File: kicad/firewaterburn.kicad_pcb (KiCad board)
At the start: 2 copper layers, 105.2 x 79 mm, 72 parts, among them J1 AudioJack2_SwitchT, J2 AudioJack2_SwitchT, J3 Conn_01x03, J4 AudioJack2_SwitchT, J5 AudioJack2_SwitchT, J6 AudioJack2_SwitchT, J7 AudioJack2_SwitchT, J8 RVT50HQBNWC00, P1 USB_C_Plug_USB2.0, Q1 DMN61D9UWQ-13, Q2 DMP31D0U-7, Q5 DMN2004WK-7, U1 RT9471GQW, U2 MCP1663T-E/MNY, U3 MCP1603-330I/MC, U4 BL654, U5 CP2102N-Axx-xQFN28

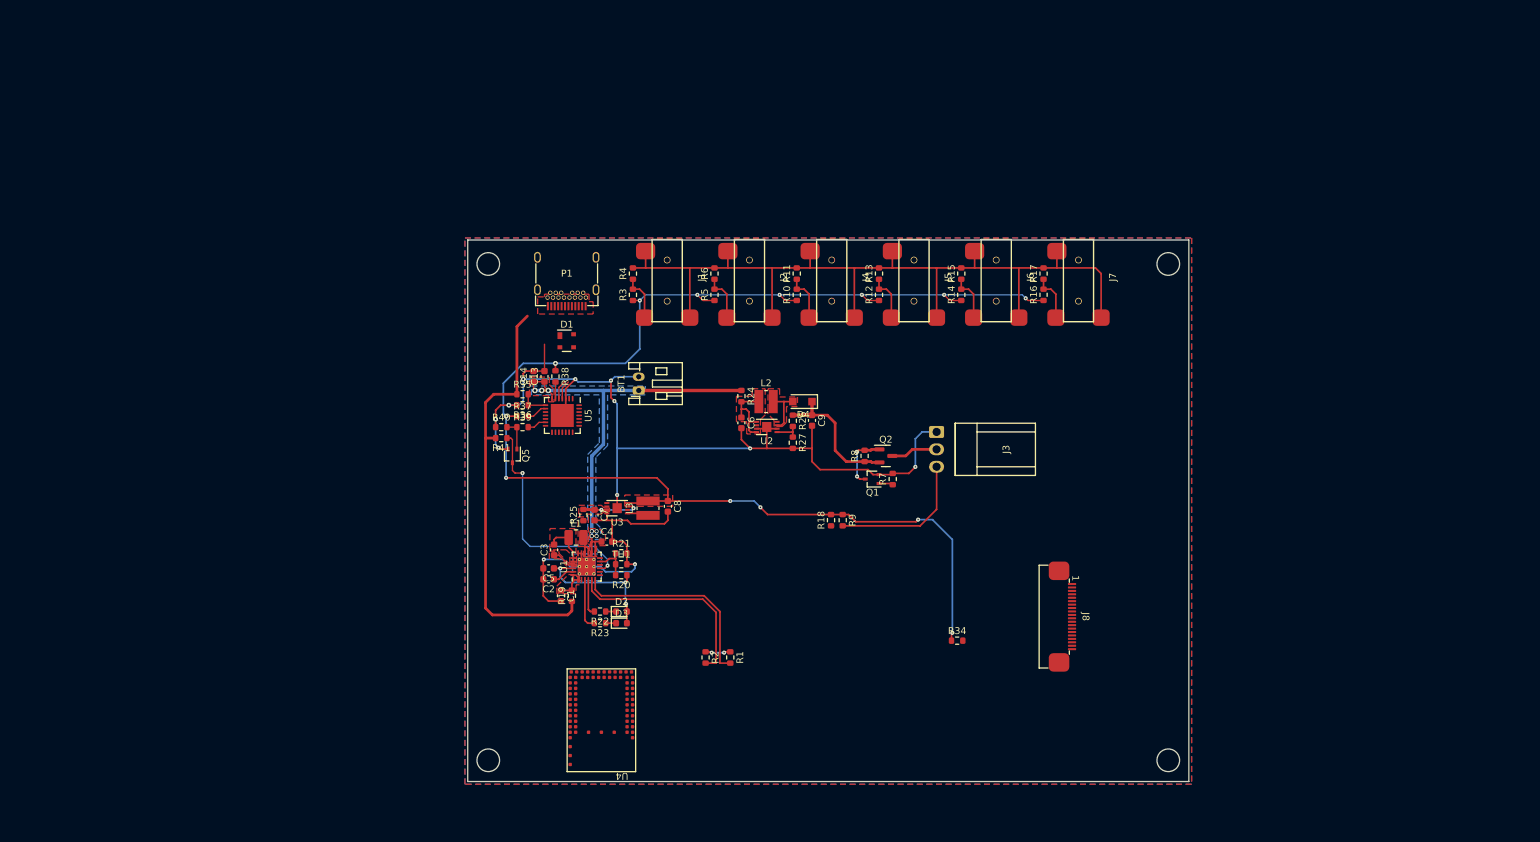
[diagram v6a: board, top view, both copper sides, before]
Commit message: add all digikeys numbers to schematic
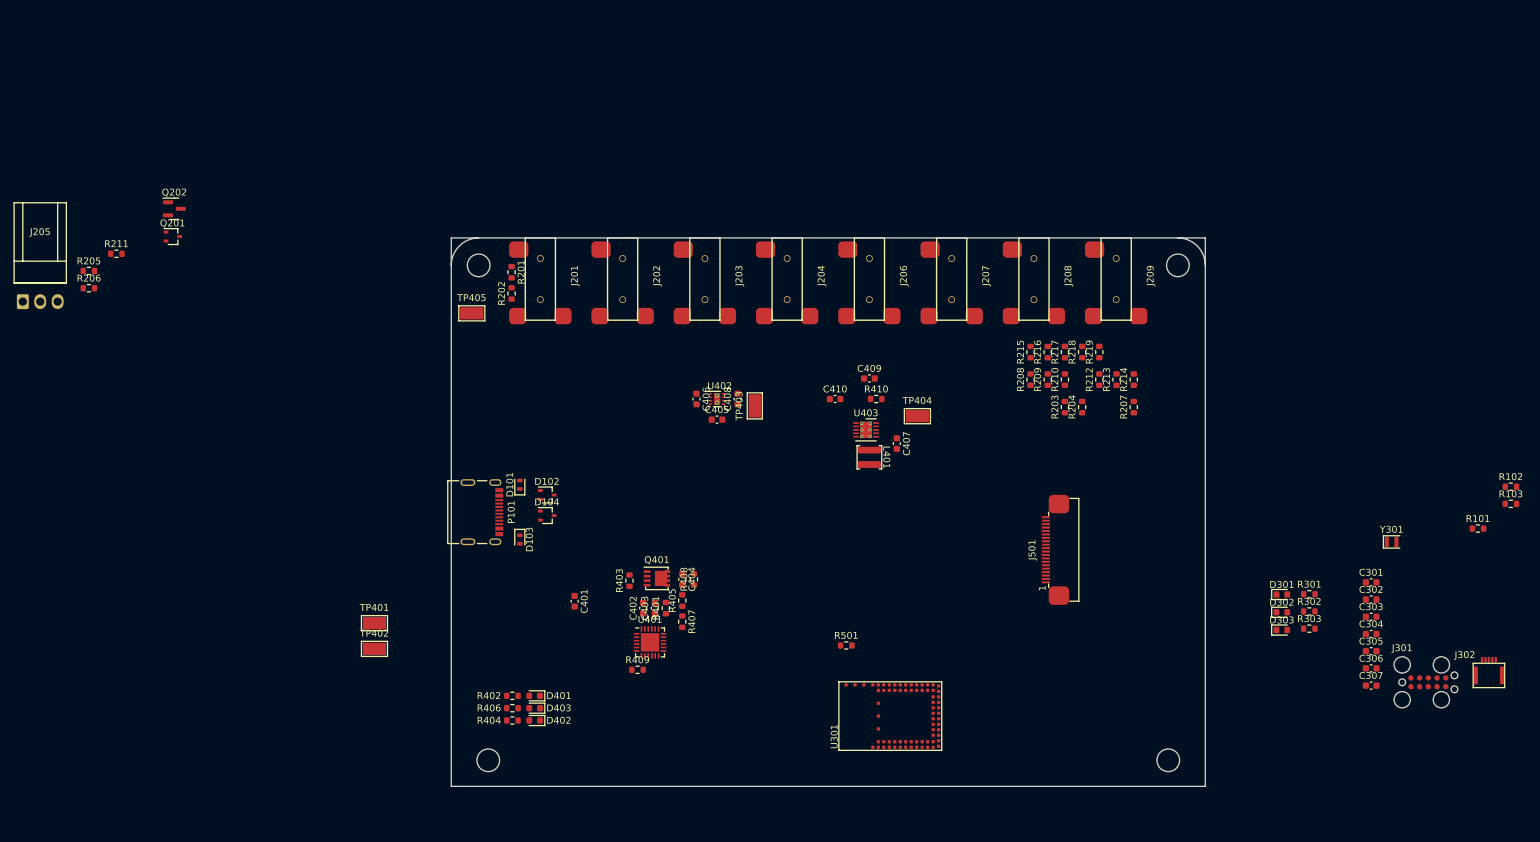
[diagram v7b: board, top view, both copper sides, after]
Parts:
- removed BT1: Battery_Cell, Connector_JST:JST_PH_S2B-PH-K_1x02_P2.00mm_Horizontal
- removed C1: 1µ, Capacitor_SMD:C_0603_1608Metric
- removed C13, C5, C7, C8: 4,7µ, Capacitor_SMD:C_0603_1608Metric
- removed C14: 100n, Capacitor_SMD:C_0603_1608Metric
- removed C2, C4, C6, C9: 10µ, Capacitor_SMD:C_0603_1608Metric
- removed C3: 47nF, Capacitor_SMD:C_0603_1608Metric
- removed D1: SP0503BAHTG, Package_TO_SOT_SMD:SOT-143
- removed D2, D3: LED, LED_SMD:LED_0603_1608Metric
- removed D4: PMEG4010ER, Diode_SMD:D_SOD-123F
- removed J1, J2, J4, J5, J6, J7: AudioJack2_SwitchT, mylib_connector:MJ-2523
- removed J3: Conn_01x03, z_connector:Molex_KK-254_AE-6410-03A_1x03_P2.54mm_Vertical
- removed J8: RVT50HQBNWC00, mylib_connector:FPC_BOTTOM_20POS_Würth_68712014522
- removed L1: 1µ, Inductor_SMD:L_1008_2520Metric
- removed L2, L3: 4µ7, Inductor_SMD:L_Wuerth_MAPI-3015
- removed P1: USB_C_Plug_USB2.0, mylib_connector:USB_C_Receptacle_Amphenol_12401548E4-2A
- removed Q1: DMN61D9UWQ-13, Package_TO_SOT_SMD:SOT-323_SC-70
- removed Q2: DMP31D0U-7, Package_TO_SOT_SMD:SOT-23
- removed Q5: DMN2004WK-7, Package_TO_SOT_SMD:SOT-323_SC-70
- removed R1, R2: 1k, Resistor_SMD:R_0603_1608Metric
- removed R10, R12, R14, R16, R3, R5: 4k42, Resistor_SMD:R_0603_1608Metric
- removed R11, R13, R15, R17, R4, R6: 3k4, Resistor_SMD:R_0603_1608Metric
- removed R18, R41, R9: 10k, Resistor_SMD:R_0603_1608Metric
- removed R19, R24, R25, R34, R38, R39: 0R, Resistor_SMD:R_0603_1608Metric
- removed R20: 5k23, Resistor_SMD:R_0603_1608Metric
- removed R21: 30k1, Resistor_SMD:R_0603_1608Metric
- removed R22, R23: 2k2, Resistor_SMD:R_0603_1608Metric
- removed R26: 1050k, Resistor_SMD:R_0603_1608Metric
- removed R27: 120k, Resistor_SMD:R_0603_1608Metric
- removed R35: 22k1, Resistor_SMD:R_0603_1608Metric
- removed R36: 47k5, Resistor_SMD:R_0603_1608Metric
- removed R37: 2k, Resistor_SMD:R_0603_1608Metric
- removed R40: 1M, Resistor_SMD:R_0603_1608Metric
- removed R7, R8: 4k7, Resistor_SMD:R_0603_1608Metric
- removed TH1: NTCG163JH103JT1, Resistor_SMD:R_0603_1608Metric
- removed U1: RT9471GQW, mylib_ic:WQFN-24-1EP_4x4mm_P0.5mm_EP2.6x2.6mm_ThermalVias
- removed U2: MCP1663T-E/MNY, Package_DFN_QFN:DFN-8-1EP_3x2mm_P0.5mm_EP1.36x1.46mm
- removed U3: MCP1603-330I/MC, Package_DFN_QFN:DFN-8-1EP_3x2mm_P0.5mm_EP1.36x1.46mm
- removed U4: BL654, mylib_ic:BL654
- removed U5: CP2102N-Axx-xQFN28, Package_DFN_QFN:QFN-28-1EP_5x5mm_P0.5mm_EP3.35x3.35mm
- added C301: 10µ, Capacitor_SMD:C_0603_1608Metric, F.Cu at (229.2, 110.2)
- added C302: 100nF, Capacitor_SMD:C_0603_1608Metric, F.Cu at (229.2, 112.8)
- added C303: 4µ7, Capacitor_SMD:C_0603_1608Metric, F.Cu at (229.2, 115.3)
- added C304: 300p, Capacitor_SMD:C_0603_1608Metric, F.Cu at (229.2, 117.8)
- added C305: 9p, Capacitor_SMD:C_0603_1608Metric, F.Cu at (229.2, 120.3)
- added C306: 300p, Capacitor_SMD:C_0603_1608Metric, F.Cu at (229.2, 122.8)
- added C307: 9p, Capacitor_SMD:C_0603_1608Metric, F.Cu at (229.2, 125.3)
- added C401: 1µ, Capacitor_SMD:C_0603_1608Metric, F.Cu at (113.0, 113.0)
- added C402: 1µ, Capacitor_SMD:C_0603_1608Metric, F.Cu at (123.0, 114.0)
- added C403: 1µ, Capacitor_SMD:C_0603_1608Metric, F.Cu at (124.7, 114.0)
- added C404: 100nF, Capacitor_SMD:C_0603_1608Metric, F.Cu at (128.7, 109.8)
- added C405: 10µ, Capacitor_SMD:C_0603_1608Metric, F.Cu at (133.8, 86.5)
- added C406: 1µ, Capacitor_SMD:C_0603_1608Metric, F.Cu at (130.8, 83.5)
- added C407: 0.47µ, Capacitor_SMD:C_0603_1608Metric, F.Cu at (160.0, 90.0)
- added C408: 10µ, Capacitor_SMD:C_0603_1608Metric, F.Cu at (136.8, 83.5)
- added C409: 22µ, Capacitor_SMD:C_0603_1608Metric, F.Cu at (156.0, 80.5)
- added C410: 4µ7, Capacitor_SMD:C_0603_1608Metric, F.Cu at (151.0, 83.5)
- added D101: ESDA25P35, mylib_ic:D_0604_1610Metric, F.Cu at (105.0, 96.0)
- added D102: ESDA25W, Package_TO_SOT_SMD:SOT-323_SC-70, F.Cu at (109.0, 97.5)
- added D103: ESDA25P35, mylib_ic:D_0604_1610Metric, F.Cu at (105.0, 104.0)
- added D104: ESDA25W, Package_TO_SOT_SMD:SOT-323_SC-70, F.Cu at (109.0, 100.5)
- added D301: LED, LED_SMD:LED_0603_1608Metric, F.Cu at (216.2, 112.0)
- added D302: LED, LED_SMD:LED_0603_1608Metric, F.Cu at (216.2, 114.6)
- added D303: LED, LED_SMD:LED_0603_1608Metric, F.Cu at (216.2, 117.2)
- added D401: LED, LED_SMD:LED_0603_1608Metric, F.Cu at (107.2, 126.8)
- added D402: LED, LED_SMD:LED_0603_1608Metric, F.Cu at (107.2, 130.4)
- added D403: LED, LED_SMD:LED_0603_1608Metric, F.Cu at (107.2, 128.6)
- added J201: AudioJack2_SwitchT, mylib_connector:MJ-2523, F.Cu at (108.0, 60.0)
- added J202: AudioJack2_SwitchT, mylib_connector:MJ-2523, F.Cu at (120.0, 60.0)
- added J203: AudioJack2_SwitchT, mylib_connector:MJ-2523, F.Cu at (132.0, 60.0)
- added J204: AudioJack2_SwitchT, mylib_connector:MJ-2523, F.Cu at (144.0, 60.0)
- added J205: Conn_01x03, mylib_connector:Molex_KK-254_AE-6410-03A_1x03_P2.54mm_Vertical, F.Cu at (32.5, 69.3)
- added J206: AudioJack2_SwitchT, mylib_connector:MJ-2523, F.Cu at (156.0, 60.0)
- added J207: AudioJack2_SwitchT, mylib_connector:MJ-2523, F.Cu at (168.0, 60.0)
- added J208: AudioJack2_SwitchT, mylib_connector:MJ-2523, F.Cu at (180.0, 60.0)
- added J209: AudioJack2_SwitchT, mylib_connector:MJ-2523, F.Cu at (192.0, 60.0)
- added J301: TC-2050, mylib_connector:TC-2050, F.Cu at (233.7, 124.8)
- added J302: Conn_01x05, mylib_connector:Easy-On 51281-5, F.Cu at (246.4, 123.8)
- added J501: RVT50HQBNWC00, mylib_connector:FPC_BOTTOM_20POS_Würth_68712014522, F.Cu at (181.8, 105.5)
- added L401: 15µ, mylib_ic:L_TDK_VLS6045EX_VLS6045AF, F.Cu at (156.0, 92.0)
- added P101: USB_C_Plug_USB2.0, mylib_connector:USB_C_Receptacle_Molex_C_24P_SMD_RA, F.Cu at (102.0, 100.0)
- added Q201: DMN61D9UWQ-13, Package_TO_SOT_SMD:SOT-323_SC-70, F.Cu at (54.4, 59.8)
- added Q202: DMP31D0U-7, Package_TO_SOT_SMD:SOT-23, F.Cu at (54.6, 55.8)
- added Q401: SI7421DN-T1-E3, Package_SO:Vishay_PowerPAK_1212-8_Single, F.Cu at (125.0, 109.7)
- added R101: 4k7, Resistor_SMD:R_0603_1608Metric, F.Cu at (244.8, 102.4)
- added R102: 4k7, Resistor_SMD:R_0603_1608Metric, F.Cu at (249.6, 96.3)
- added R103: 4k7, Resistor_SMD:R_0603_1608Metric, F.Cu at (249.6, 98.8)
- added R201: 4k42, Resistor_SMD:R_0603_1608Metric, F.Cu at (103.8, 65.0)
- added R202: 3k4, Resistor_SMD:R_0603_1608Metric, F.Cu at (103.8, 68.1)
- added R203: 4k42, Resistor_SMD:R_0603_1608Metric, F.Cu at (184.5, 84.7)
- added R204: 3k4, Resistor_SMD:R_0603_1608Metric, F.Cu at (187.0, 84.7)
- added R205: 4k7, Resistor_SMD:R_0603_1608Metric, F.Cu at (42.1, 64.8)
- added R206: 4k7, Resistor_SMD:R_0603_1608Metric, F.Cu at (42.1, 67.3)
- added R207: 4k42, Resistor_SMD:R_0603_1608Metric, F.Cu at (194.6, 84.7)
- added R208: 3k4, Resistor_SMD:R_0603_1608Metric, F.Cu at (179.5, 80.7)
- added R209: 4k42, Resistor_SMD:R_0603_1608Metric, F.Cu at (182.0, 80.7)
- added R210: 3k4, Resistor_SMD:R_0603_1608Metric, F.Cu at (184.5, 80.7)
- added R211: 10k, Resistor_SMD:R_0603_1608Metric, F.Cu at (46.1, 62.3)
- added R212: 4k42, Resistor_SMD:R_0603_1608Metric, F.Cu at (189.5, 80.7)
- added R213: 3k4, Resistor_SMD:R_0603_1608Metric, F.Cu at (192.1, 80.7)
- added R214: 4k42, Resistor_SMD:R_0603_1608Metric, F.Cu at (194.6, 80.7)
- added R215: 3k4, Resistor_SMD:R_0603_1608Metric, F.Cu at (179.5, 76.7)
- added R216: 4k42, Resistor_SMD:R_0603_1608Metric, F.Cu at (182.0, 76.7)
- added R217: 3k4, Resistor_SMD:R_0603_1608Metric, F.Cu at (184.5, 76.7)
- added R218: 4k42, Resistor_SMD:R_0603_1608Metric, F.Cu at (187.0, 76.7)
- added R219: 3k4, Resistor_SMD:R_0603_1608Metric, F.Cu at (189.5, 76.7)
- added R301: 1k, Resistor_SMD:R_0603_1608Metric, F.Cu at (220.2, 112.0)
- added R302: 1k, Resistor_SMD:R_0603_1608Metric, F.Cu at (220.2, 114.5)
- added R303: 1k, Resistor_SMD:R_0603_1608Metric, F.Cu at (220.2, 117.0)
- added R401: 1k, Resistor_SMD:R_0603_1608Metric, F.Cu at (126.3, 114.0)
- added R402: 1k, Resistor_SMD:R_0603_1608Metric, F.Cu at (103.9, 126.8)
- added R403: 100k, Resistor_SMD:R_0603_1608Metric, F.Cu at (121.0, 110.0)
- added R404: 1k, Resistor_SMD:R_0603_1608Metric, F.Cu at (103.9, 130.4)
- added R405: 100, Resistor_SMD:R_0603_1608Metric, F.Cu at (128.7, 112.9)
- added R406: 1k, Resistor_SMD:R_0603_1608Metric, F.Cu at (103.9, 128.6)
- added R407: 22k, Resistor_SMD:R_0603_1608Metric, F.Cu at (128.7, 116.0)
- added R408: 1k, Resistor_SMD:R_0603_1608Metric, F.Cu at (130.4, 109.8)
- added R409: 100k, Resistor_SMD:R_0603_1608Metric, F.Cu at (122.2, 123.0)
- added R410: 215k, Resistor_SMD:R_0603_1608Metric, F.Cu at (157.0, 83.5)
- added R501: 0R, Resistor_SMD:R_0603_1608Metric, F.Cu at (152.6, 119.5)
- added TP401: TestPoint, TestPoint:TestPoint_Keystone_5015_Micro-Minature, F.Cu at (83.8, 116.2)
- added TP402: TestPoint, TestPoint:TestPoint_Keystone_5015_Micro-Minature, F.Cu at (83.8, 120.0)
- added TP403: TestPoint, TestPoint:TestPoint_Keystone_5015_Micro-Minature, F.Cu at (139.3, 84.5)
- added TP404: TestPoint, TestPoint:TestPoint_Keystone_5015_Micro-Minature, F.Cu at (163.0, 86.0)
- added TP405: TestPoint, TestPoint:TestPoint_Keystone_5015_Micro-Minature, F.Cu at (98.0, 71.0)
- added U301: BL654, mylib_ic:BL654, F.Cu at (166.6, 124.8)
- added U401: STUSB4500QTR, Package_DFN_QFN:QFN-24-1EP_4x4mm_P0.5mm_EP2.7x2.7mm, F.Cu at (124.0, 119.0)
- added U402: LM2775DSG, Package_SON:WSON-8-1EP_2x2mm_P0.5mm_EP0.9x1.6mm_ThermalVias, F.Cu at (133.8, 83.5)
- added U403: LT3973-3.3, Package_DFN_QFN:DFN-10-1EP_3x3mm_P0.5mm_EP1.65x2.38mm_ThermalVias, F.Cu at (155.5, 88.0)
- added Y301: Crystal, mylib_ic:CM8V-T1A-2Pin_2.0x1.2mm, F.Cu at (232.2, 104.3)
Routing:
- net GND: track 307.0 -> 0.00 mm, vias 12 -> 0
- net +3V3: track 211.8 -> 0.00 mm, vias 15 -> 0
- net VAA: track 65.7 -> 0.00 mm, vias 7 -> 0
- net VBUS: track 63.2 -> 0.00 mm
- net /USB<->UART/CHREN: track 32.4 -> 0.00 mm, vias 2 -> 0
- net /power unit/CHARGER_SCL: track 30.0 -> 0.00 mm
- net /power unit/CHARGER_SDA: track 29.9 -> 0.00 mm
- net Net-(C5-Pad1): track 21.1 -> 0.00 mm, vias 3 -> 0
- net /OUTPUT/TACHO: track 20.9 -> 0.00 mm
- net +12V: track 19.8 -> 0.00 mm
- net Net-(C6-Pad1): track 11.1 -> 0.00 mm
- net Net-(C7-Pad1): track 9.23 -> 0.00 mm, vias 2 -> 0
- net Net-(Q1-Pad3): track 8.36 -> 0.00 mm, vias 2 -> 0
- net /power unit/~{PG}: track 7.45 -> 0.00 mm
- net Net-(D4-Pad2): track 7.09 -> 0.00 mm
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- removed copper zone on F.Cu, net +3V3
- removed copper zone on B.Cu, net GND
- removed copper zone on F.Cu, net GND
- removed copper zone on F.Cu, net Net-(C1-Pad1)
- removed copper zone on F.Cu, net Net-(C3-Pad1)
- removed copper zone on F.Cu, net Net-(C3-Pad2)
- removed copper zone on F.Cu, net Net-(C6-Pad1)
- removed copper zone on F.Cu, net Net-(C7-Pad1)
- removed copper zone on F.Cu, net Net-(D4-Pad2)
- removed copper zone on B.Cu, net VAA
- removed copper zone on F.Cu, net VAA
- removed copper zone on F.Cu, net VS
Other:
- board size 105.2 x 79 mm -> 110 x 80 mm

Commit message: wip
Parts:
- removed D103: ESDA25P35, mylib_ic:D_0604_1610Metric
- removed D104: ESDA25W, Package_TO_SOT_SMD:SOT-323_SC-70
- removed J208, J209: AudioJack2_SwitchT, mylib_connector:MJ-2523
- removed R216, R218: 4k42, Resistor_SMD:R_0603_1608Metric
- removed R217, R219: 3k4, Resistor_SMD:R_0603_1608Metric
- added U101: TPD4E02B04DQA, Package_SON:USON-10_2.5x1.0mm_P0.5mm, F.Cu at (90.2, 80.8)
- C304: value 300p -> 9p
- C307: value 9p -> 300p
- C401: value 1µ -> 100nF
- C402: value 1µ -> 0.47µ
- C404: value 100nF -> 4µ7
- C405: value 10µ -> 22µ
- C407: value 0.47µ -> 1µ
- C409: value 22µ -> 1µ
- C410: value 4µ7 -> 10µ
- D102: value ESDA25W -> ESDA25P35; footprint Package_TO_SOT_SMD:SOT-323_SC-70 -> mylib_ic:D_0604_1610Metric
- J205: value Conn_01x03 -> AudioJack2_SwitchT; footprint mylib_connector:Molex_KK-254_AE-6410-03A_1x03_P2.54mm_Vertical -> mylib_connector:MJ-2523
- J207: value AudioJack2_SwitchT -> Conn_01x03; footprint mylib_connector:MJ-2523 -> mylib_connector:Molex_KK-254_AE-6410-03A_1x03_P2.54mm_Vertical
- J301: value TC-2050 -> Conn_01x05; footprint mylib_connector:TC-2050 -> mylib_connector:Easy-On 51281-5
- J302: value Conn_01x05 -> TC-2050; footprint mylib_connector:Easy-On 51281-5 -> mylib_connector:TC-2050
- Q201: value DMN61D9UWQ-13 -> DMP31D0U-7; footprint Package_TO_SOT_SMD:SOT-323_SC-70 -> Package_TO_SOT_SMD:SOT-23
- Q202: value DMP31D0U-7 -> DMN61D9UWQ-13; footprint Package_TO_SOT_SMD:SOT-23 -> Package_TO_SOT_SMD:SOT-323_SC-70
- R202, R208: value 3k4 -> 4k42
- R205, R206: value 4k7 -> 3k4
- R211: value 10k -> 3k4
- R212: value 4k42 -> 3k4
- R213, R215: value 3k4 -> 4k7
- R214: value 4k42 -> 10k
- R402: value 1k -> 100k
- R403, R409: value 100k -> 1k
- R404: value 1k -> 100
- R405: value 100 -> 22k
- R406: value 1k -> 215k
- R407: value 22k -> 100k
- R410: value 215k -> 1k
- U401: value STUSB4500QTR -> LT3973-3.3; footprint Package_DFN_QFN:QFN-24-1EP_4x4mm_P0.5mm_EP2.7x2.7mm -> Package_DFN_QFN:DFN-10-1EP_3x3mm_P0.5mm_EP1.65x2.38mm_ThermalVias
- U402: value LM2775DSG -> STUSB4500QTR; footprint Package_SON:WSON-8-1EP_2x2mm_P0.5mm_EP0.9x1.6mm_ThermalVias -> Package_DFN_QFN:QFN-24-1EP_4x4mm_P0.5mm_EP2.7x2.7mm_ThermalVias
- U403: value LT3973-3.3 -> LM2775DSG; footprint Package_DFN_QFN:DFN-10-1EP_3x3mm_P0.5mm_EP1.65x2.38mm_ThermalVias -> Package_SON:WSON-8-1EP_2x2mm_P0.5mm_EP0.9x1.6mm_ThermalVias
- moved J205 138.9 mm to (171.1, 60.0)
- moved J301 138.6 mm to (101.2, 84.1)
- moved Q201 127.0 mm to (180.8, 72.6)
- moved Q202 127.0 mm to (181.0, 68.5)
- moved R205 120.4 mm to (147.4, 123.4)
- moved R206 120.4 mm to (147.4, 125.9)
- moved R211 120.4 mm to (151.4, 120.9)
- moved R213 112.1 mm to (81.0, 65.2)
- moved R214 111.3 mm to (84.0, 68.2)
- moved R212 109.2 mm to (81.0, 68.3)
- moved R210 108.6 mm to (77.0, 65.2)
- moved R209 105.7 mm to (77.0, 68.3)
- moved R207 102.9 mm to (93.0, 67.9)
- moved R102 100.1 mm to (155.7, 130.9)
- moved R301 98.4 mm to (122.8, 98.0), turned to 90 degrees
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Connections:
- net /mcu_n_tft/D+ renamed /D+
- net /mcu_n_tft/D- renamed /D-
- C304 pad 1: Net-(J302-Pin_2) -> GND
- C304 pad 2: GND -> /mcu_n_tft/XL1
- C305 pad 1: GND -> /mcu_n_tft/XL2
- C305 pad 2: /mcu_n_tft/XL1 -> GND
- C306 pad 1: Net-(J302-Pin_4) -> Net-(J301-Pin_2)
- C307 pad 1: /mcu_n_tft/XL2 -> Net-(J301-Pin_4)
- C401 pad 1: VBUS -> VDD
- C401 pad 2: GND -> Net-(C401-Pad2)
- C402 pad 1: Net-(U401-VREG_2V7) -> Net-(U401-BOOST)
- C402 pad 2: GND -> Net-(U401-SW)
- C403 pad 1: Net-(U401-VREG_1V2) -> VBUS
- C404 pad 2: Net-(C404-Pad2) -> GND
- C406 pad 1: Net-(U402-C1-) -> Net-(U402-VREG_2V7)
- C406 pad 2: Net-(U402-C1+) -> GND
- C407 pad 1: Net-(U403-BOOST) -> Net-(U402-VREG_1V2)
- C407 pad 2: Net-(U403-SW) -> GND
- C408 pad 1: +5V -> +3V3
- C409 pad 1: +3V3 -> Net-(U403-C1-)
- C409 pad 2: GND -> Net-(U403-C1+)
- C410 pad 1: VDD -> +5V
- D102 pad 1: /pwr_supply/CC2 -> VBUS
- D102 pad 2: /pwr_supply/CC1 -> GND
- J201 pad T: /OUTPUT/probe1 -> /OUTPUT/probe0
- J202 pad T: /OUTPUT/probe5 -> /OUTPUT/probe1
- J204 pad T: /OUTPUT/probe6 -> /OUTPUT/probe3
- J206 pad T: /OUTPUT/probe3 -> /OUTPUT/probe5
- J301 pad 1: +3V3 -> unconnected-(J301-Pin_1-Pad1)
- J301 pad 2: /mcu_n_tft/SWDIO -> Net-(J301-Pin_2)
- J301 pad 3: GND -> unconnected-(J301-Pin_3-Pad3)
- J301 pad 4: /mcu_n_tft/SWCLK -> Net-(J301-Pin_4)
- J301 pad 5: GND -> unconnected-(J301-Pin_5-Pad5)
- J302 pad 1: unconnected-(J302-Pin_1-Pad1) -> +3V3
- J302 pad 2: Net-(J302-Pin_2) -> /mcu_n_tft/SWDIO
- J302 pad 3: unconnected-(J302-Pin_3-Pad3) -> GND
- J302 pad 4: Net-(J302-Pin_4) -> /mcu_n_tft/SWCLK
- J302 pad 5: unconnected-(J302-Pin_5-Pad5) -> GND
- L401 pad 1: Net-(U403-SW) -> Net-(U401-SW)
- Q201 pad 1: /OUTPUT/PWM -> Net-(Q201-G)
- Q201 pad 2: GND -> +12V
- Q201 pad 3: Net-(Q201-D) -> Net-(J207-Pin_2)
- Q202 pad 1: Net-(Q201-D) -> /OUTPUT/PWM
- Q202 pad 2: +12V -> GND
- Q202 pad 3: Net-(J205-Pin_2) -> Net-(Q201-G)
- R201 pad 2: /OUTPUT/probe1 -> /OUTPUT/probe0
- R202 pad 1: /OUTPUT/probe1 -> +3V3
- R202 pad 2: GND -> /OUTPUT/probe1
- R203 pad 2: /OUTPUT/probe5 -> /OUTPUT/probe2
- R204 pad 1: /OUTPUT/probe5 -> /OUTPUT/probe0
- R205 pad 1: /OUTPUT/PWM -> /OUTPUT/probe1
- R206 pad 1: +12V -> /OUTPUT/probe2
- R206 pad 2: Net-(Q201-D) -> GND
- R207 pad 2: /OUTPUT/probe2 -> /OUTPUT/probe3
- R208 pad 1: /OUTPUT/probe2 -> +3V3
- R208 pad 2: GND -> /OUTPUT/probe4
- R209 pad 2: /OUTPUT/probe6 -> /OUTPUT/probe5
- R210 pad 1: /OUTPUT/probe6 -> /OUTPUT/probe3
- R211 pad 1: +3V3 -> /OUTPUT/probe4
- R211 pad 2: /OUTPUT/TACHO -> GND
- R212 pad 1: +3V3 -> /OUTPUT/probe5
- R212 pad 2: /OUTPUT/probe3 -> GND
- R213 pad 1: /OUTPUT/probe3 -> +12V
- R213 pad 2: GND -> Net-(Q201-G)
- R214 pad 2: /OUTPUT/probe7 -> /OUTPUT/TACHO
- R215 pad 1: /OUTPUT/probe7 -> /OUTPUT/PWM
- R401 pad 1: Net-(U401-VBUS_VS_DISCH) -> Net-(U402-VBUS_VS_DISCH)
- R402 pad 1: Net-(D401-A) -> Net-(Q401-G)
- R402 pad 2: +3V3 -> VBUS
- R403 pad 1: Net-(Q401-G) -> Net-(U402-DISCH)
- R403 pad 2: VBUS -> VDD
- R404 pad 1: Net-(D402-A) -> Net-(Q401-G)
- R404 pad 2: +3V3 -> Net-(C401-Pad2)
- R405 pad 2: Net-(C404-Pad2) -> Net-(U402-VBUS_EN_SNK)
- R406 pad 1: Net-(D403-A) -> Net-(U401-RT)
- R406 pad 2: +3V3 -> GND
- R407 pad 1: Net-(Q401-G) -> Net-(U402-RESET)
- R407 pad 2: Net-(U401-VBUS_EN_SNK) -> GND
- R408 pad 1: Net-(U401-DISCH) -> Net-(D401-A)
- R408 pad 2: VDD -> +3V3
- R409 pad 1: Net-(U401-RESET) -> Net-(D402-A)
- R409 pad 2: GND -> +3V3
- R410 pad 1: Net-(U403-RT) -> Net-(D403-A)
- R410 pad 2: GND -> +3V3
- TP401 pad 1: VBUS -> GND
- TP402 pad 1: VDD -> VBUS
- TP403 pad 1: +5V -> VDD
- TP405 pad 1: GND -> +5V
- U301 pad 44: /OUTPUT/probe8 -> /mcu_n_tft/ADC_7
- U301 pad 57: Net-(J302-Pin_4) -> Net-(J301-Pin_4)
- U301 pad 59: Net-(J302-Pin_2) -> Net-(J301-Pin_2)
- U401 pad 1: /pwr_supply/CC1 -> +3V3
- U401 pad 10: GND -> Net-(U401-RT)
- U401 pad 11: unconnected-(U401-ATTACH-Pad11) -> GND
- U401 pad 2: /pwr_supply/CC1 -> +3V3
- U401 pad 3: unconnected-(U401-NC-Pad3) -> VDD
- U401 pad 4: /pwr_supply/CC2 -> VDD
- U401 pad 5: /pwr_supply/CC2 -> GND
- U401 pad 6: Net-(U401-RESET) -> Net-(U401-SW)
- U401 pad 7: /mcu_n_tft/SCL -> Net-(U401-BOOST)
- U401 pad 8: /mcu_n_tft/SDA -> +3V3
- U401 pad 9: Net-(U401-DISCH) -> unconnected-(U401-PG-Pad9)
- U402 pad 1: +3V3 -> /pwr_supply/CC1
- U402 pad 2: Net-(U402-C1-) -> /pwr_supply/CC1
- U402 pad 3: Net-(U402-C1+) -> unconnected-(U402-NC-Pad3)
- U402 pad 4: +3V3 -> /pwr_supply/CC2
- U402 pad 5: +3V3 -> /pwr_supply/CC2
- U402 pad 6: +5V -> Net-(U402-RESET)
- U402 pad 7: +3V3 -> /mcu_n_tft/SCL
- U402 pad 8: GND -> /mcu_n_tft/SDA
- U402 pad 9: GND -> Net-(U402-DISCH)
- U403 pad 2: +3V3 -> Net-(U403-C1-)
- U403 pad 3: VDD -> Net-(U403-C1+)
- U403 pad 4: VDD -> +3V3
- U403 pad 5: GND -> +3V3
- U403 pad 6: Net-(U403-SW) -> +5V
- U403 pad 7: Net-(U403-BOOST) -> +3V3
- U403 pad 8: +3V3 -> GND
- U403 pad 9: unconnected-(U403-PG-Pad9) -> GND
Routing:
- net +3V3: track 0.00 -> 29.3 mm, vias 0 -> 6
- net GND: track 0.00 -> 9.05 mm
- net /D+: track 0.00 -> 6.96 mm
- net /D-: track 0.00 -> 6.48 mm, vias 0 -> 2
- net VBUS: track 0.00 -> 5.93 mm
- net Net-(U403-SW): track 0.00 -> 5.15 mm
- net +5V: track 0.00 -> 4.31 mm
- net /pwr_supply/CC2: track 0.00 -> 4.29 mm, vias 0 -> 2
- net Net-(U402-VREG_2V7): track 0.00 -> 2.29 mm
- net Net-(D403-A): track 0.00 -> 2.29 mm
- net Net-(U402-VREG_1V2): track 0.00 -> 2.27 mm
- net /pwr_supply/CC1: track 0.00 -> 1.47 mm
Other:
- board size 110 x 80 mm -> 90 x 50 mm
- copper layers 2 -> 4
